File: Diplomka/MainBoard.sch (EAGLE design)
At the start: 29 parts, among them K1 ARK550/2, K2 ARK550/2, Q1 AP2012P3C-P22, Q2 BC817-40LT1SMD, U1 ESP32-WROOM-32, U2 AMS1117-3.3

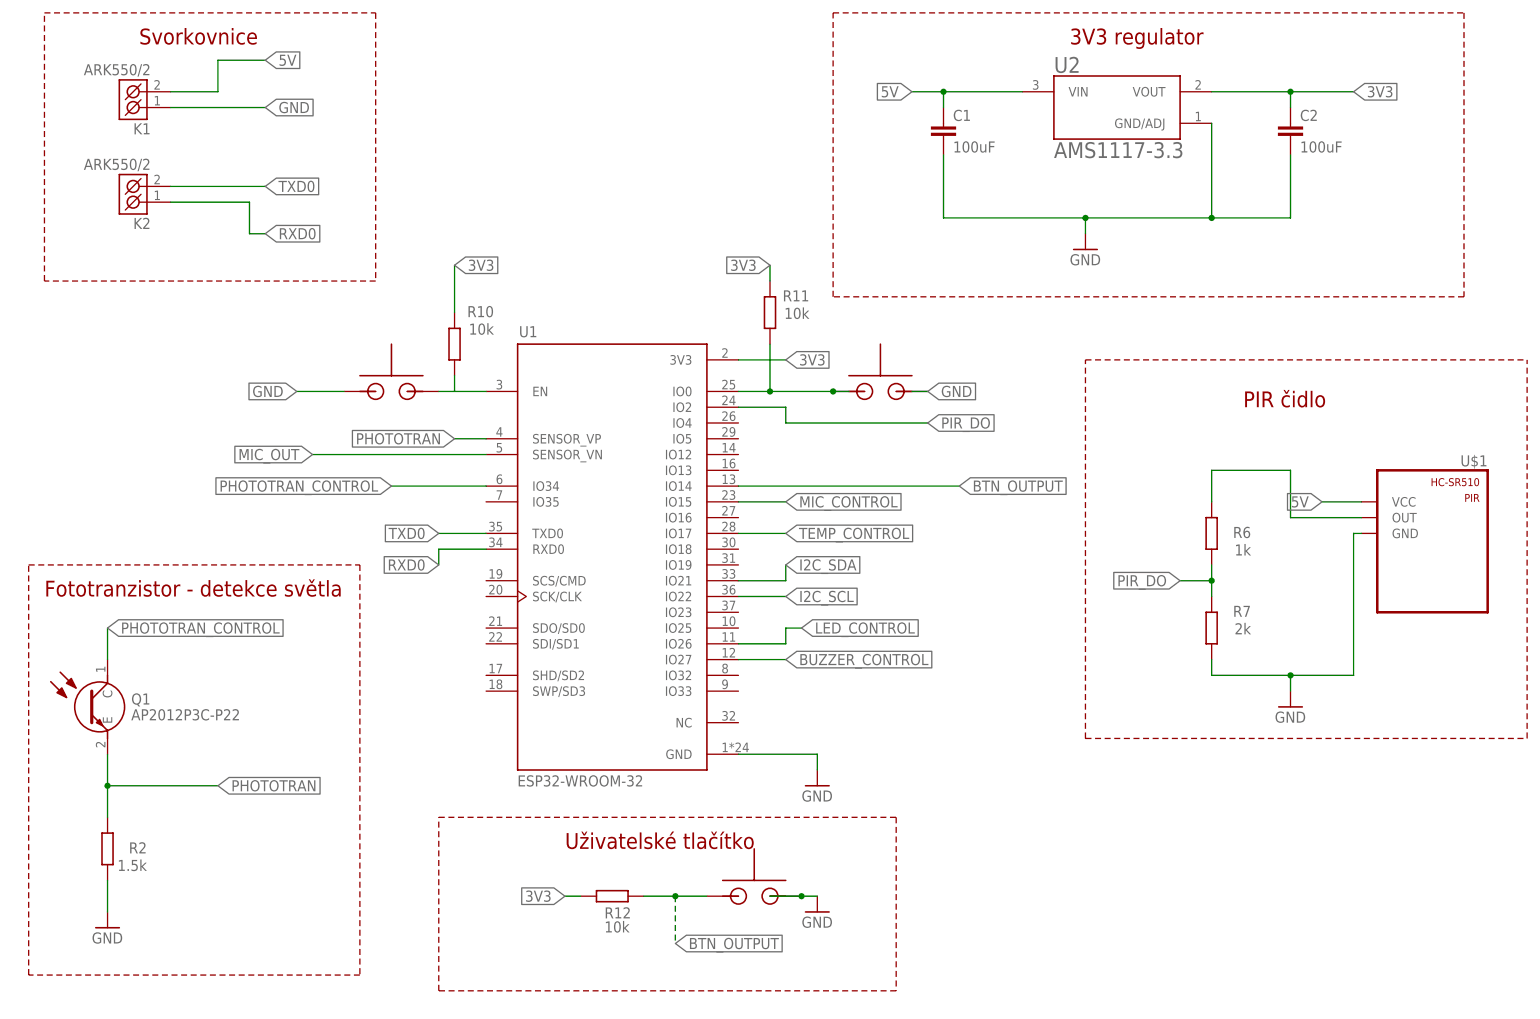
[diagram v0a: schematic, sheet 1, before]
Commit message: Přidány do repozitáře pravidla JLCPCB, nakresleno PCB asi z 70%ˇ.
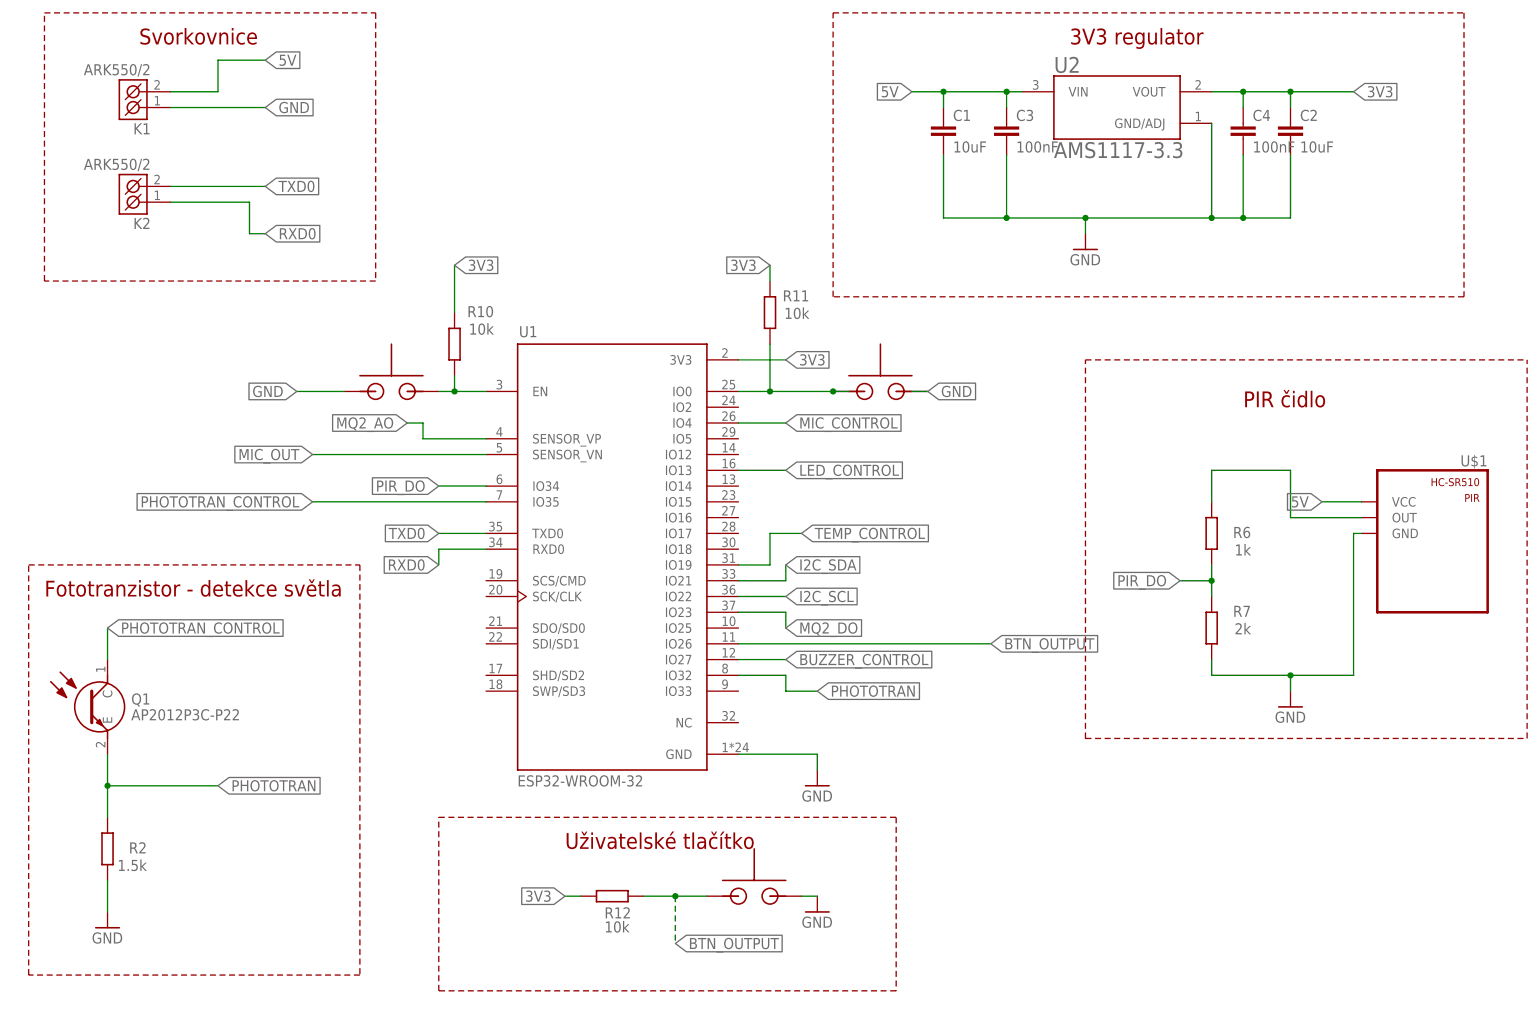
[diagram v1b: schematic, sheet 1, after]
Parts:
- added C3, C4: 100nF, rcl:C-EUC0805
- C1, C2: value 100uF -> 10uF
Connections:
- removed net N$9: R10.1
- net 3V3: now also C4.1; no longer U$3.VCC
- net 5V: now also C3.1
- net BTN_OUTPUT: now also U1.IO26; no longer U1.IO14
- net GND: now also C3.2, C4.2
- net LED_CONTROL: now also U1.IO13; no longer U1.IO26
- net MIC_CONTROL: now also U$3.VCC, U1.IO4; no longer U$3.OUT, U1.IO15
- net MIC_OUT: now also U$3.OUT
- net MQ2_AO: now also U1.SENSOR_VP
- net MQ2_DO: now also U1.IO23
- net N$7: now also R10.1
- net PHOTOTRAN: now also U1.IO32; no longer U1.SENSOR_VP
- net PHOTOTRAN_CONTROL: now also U1.IO35; no longer U1.IO34
- net PIR_DO: now also U1.IO34; no longer U1.IO2
- net TEMP_CONTROL: now also U1.IO19; no longer U1.IO17

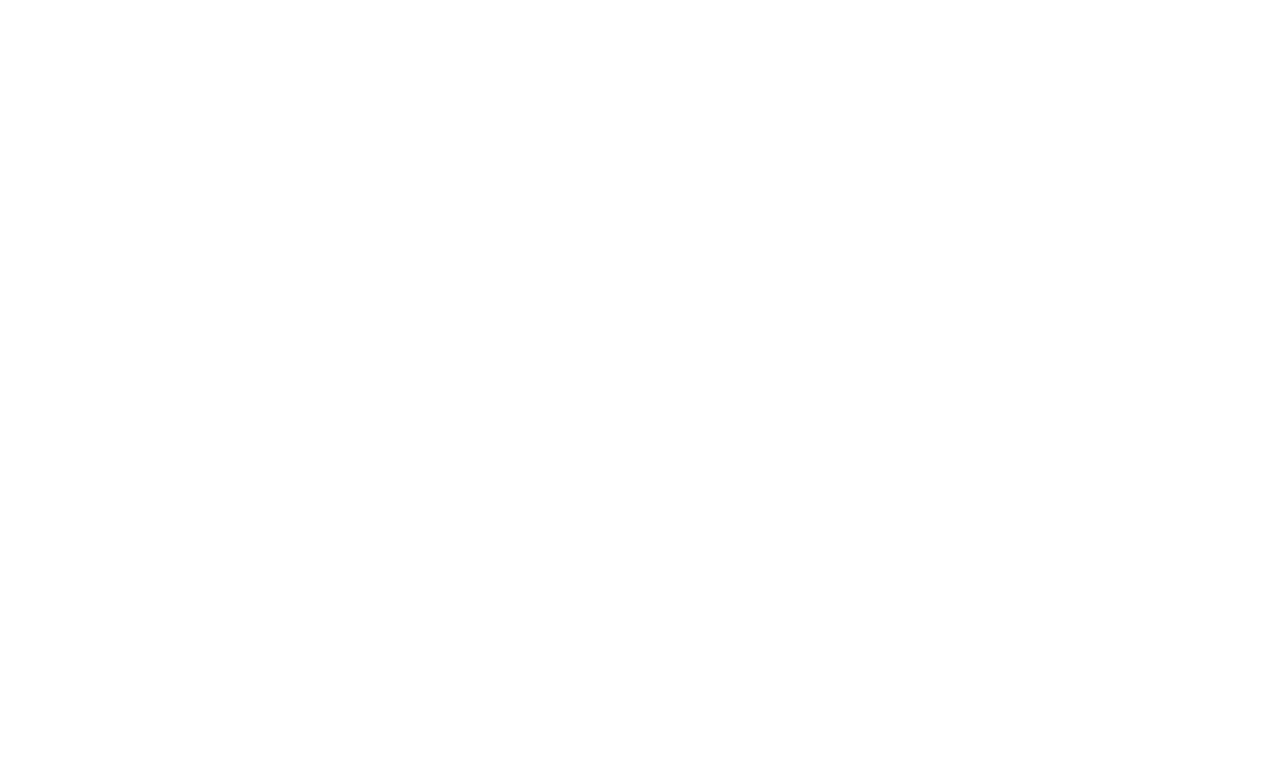
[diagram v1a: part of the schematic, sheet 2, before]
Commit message: Přidán stepdown converted. Třeba dodat vhodnou cívku a dokreslit desku.
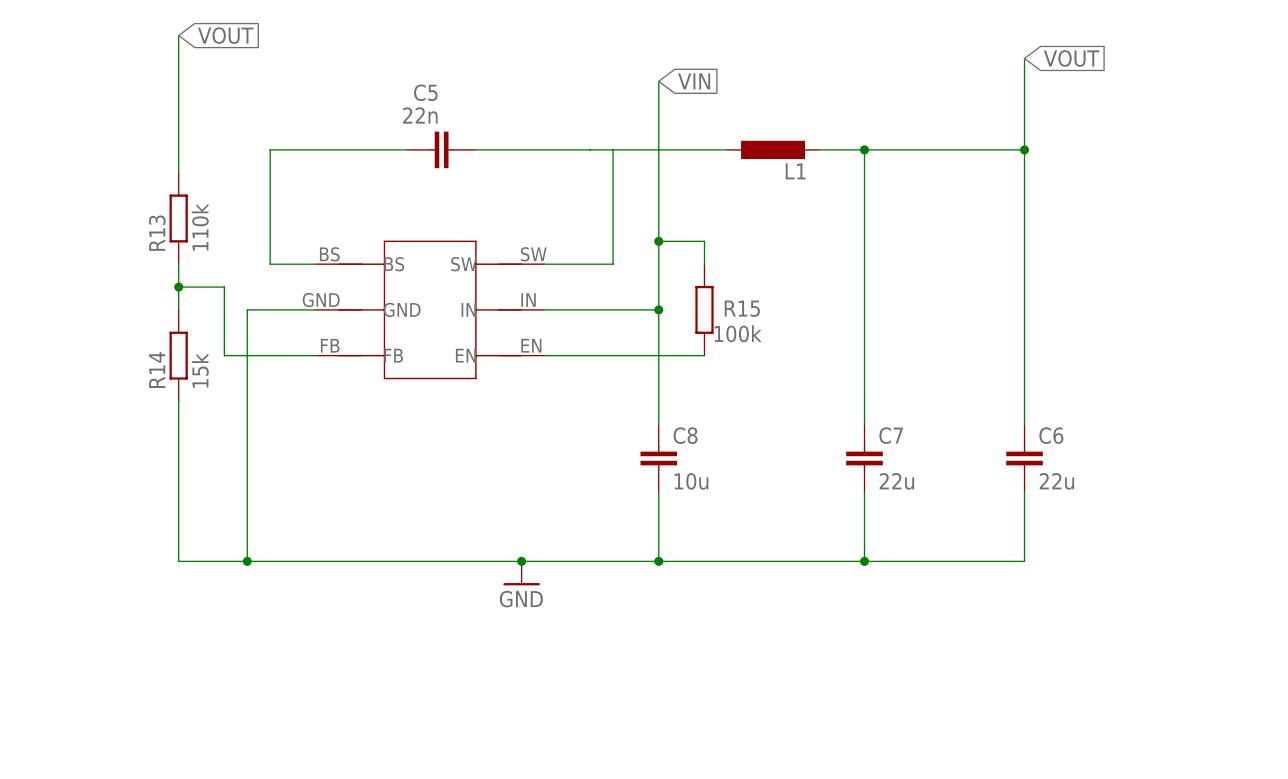
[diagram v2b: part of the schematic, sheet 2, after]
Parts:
- added C5: 22n, rcl:C-EUC0805
- added C6, C7: 22u, rcl:C-EUC0805
- added C8: 10u, rcl:C-EUC0805
- added L1: (no value), rcl:L-EUL3225M
- added R13: 110k, rcl:R-EU_R0805
- added R14: 15k, rcl:R-EU_R0805
- added R15: 100k, rcl:R-EU_R0805
- added U$9: SD8942, myParts:SD8942
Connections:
- new net N$10: C5.2, L1.1, U$9.SW
- new net N$11: R15.1, U$9.EN
- new net N$12: R13.1, R14.2, U$9.FB
- new net N$9: C5.1, U$9.BS
- new net VIN: C8.1, R15.2, U$9.IN
- new net VOUT: C6.1, C7.1, L1.2, R13.2
- net GND: now also C6.2, C7.2, C8.2, R14.1, U$9.GND
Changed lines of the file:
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@@
 <part name="C3" library="rcl" library_urn="urn:adsk.eagle:library:334" deviceset="C-EU" device="C0805" package3d_urn="urn:adsk.eagle:package:23617/2" value="100nF"/>
 <part name="C4" library="rcl" library_urn="urn:adsk.eagle:library:334" deviceset="C-EU" device="C0805" package3d_urn="urn:adsk.eagle:package:23617/2" value="100nF"/>
+<part name="U$9" library="myParts" deviceset="SD8942" device=""/>
+<part name="C5" library="rcl" library_urn="urn:adsk.eagle:library:334" deviceset="C-EU" device="C0805" package3d_urn="urn:adsk.eagle:package:23617/2" value="22n"/>
+<part name="C6" library="rcl" library_urn="urn:adsk.eagle:library:334" deviceset="C-EU" device="C0805" package3d_urn="urn:adsk.eagle:package:23617/2" value="22u"/>
+<part name="C7" library="rcl" library_urn="urn:adsk.eagle:library:334" deviceset="C-EU" device="C0805" package3d_urn="urn:adsk.eagle:package:23617/2" value="22u"/>
+<part name="C8" library="rcl" library_urn="urn:adsk.eagle:library:334" deviceset="C-EU" device="C0805" package3d_urn="urn:adsk.eagle:package:23617/2" value="10u"/>
+<part name="R13" library="rcl" library_urn="urn:adsk.eagle:library:334" deviceset="R-EU_" device="R0805" package3d_urn="urn:adsk.eagle:package:23553/2" value="110k"/>
+<part name="R14" library="rcl" library_urn="urn:adsk.eagle:library:334" deviceset="R-EU_" device="R0805" package3d_urn="urn:adsk.eagle:package:23553/2" value="15k"/>
+<part name="R15" library="rcl" library_urn="urn:adsk.eagle:library:334" deviceset="R-EU_" device="R0805" package3d_urn="urn:adsk.eagle:package:23553/2" value="100k"/>
+<part name="L1" library="rcl" library_urn="urn:adsk.eagle:library:334" deviceset="L-EU" device="L3225M" package3d_urn="urn:adsk.eagle:package:23477/2"/>
+<part name="GND9" library="supply1" library_urn="urn:adsk.eagle:library:371" deviceset="GND" device=""/>
 </parts>
 <sheets>
@@
 </instance>
 <instance part="U$5" gate="G$1" x="58.42" y="119.38" smashed="yes"/>
+<instance part="U$9" gate="G$1" x="27.94" y="220.98" smashed="yes"/>
+<instance part="C5" gate="G$1" x="27.94" y="238.76" smashed="yes" rot="R90">
+<attribute name="NAME" x="28.956" y="245.999" size="1.778" layer="95" rot="R180"/>
+<attribute name="VALUE" x="28.956" y="243.459" size="1.778" layer="96" rot="R180"/>
+</instance>
+<instance part="C6" gate="G$1" x="93.98" y="205.74" smashed="yes">
+<attribute name="NAME" x="95.504" y="206.121" size="1.778" layer="95"/>
+<attribute name="VALUE" x="95.504" y="201.041" size="1.778" layer="96"/>
+</instance>
+<instance part="C7" gate="G$1" x="76.2" y="205.74" smashed="yes">
+<attribute name="NAME" x="77.724" y="206.121" size="1.778" layer="95"/>
+<attribute name="VALUE" x="77.724" y="201.041" size="1.778" layer="96"/>
+</instance>
+<instance part="C8" gate="G$1" x="53.34" y="205.74" smashed="yes">
+<attribute name="NAME" x="54.864" y="206.121" size="1.778" layer="95"/>
+<attribute name="VALUE" x="54.864" y="201.041" size="1.778" layer="96"/>
+</instance>
+<instance part="R13" gate="G$1" x="0" y="231.14" smashed="yes" rot="R90">
+<attribute name="NAME" x="-1.4986" y="227.33" size="1.778" layer="95" rot="R90"/>
+<attribute name="VALUE" x="3.302" y="227.33" size="1.778" layer="96" rot="R90"/>
+</instance>
+<instance part="R14" gate="G$1" x="0" y="215.9" smashed="yes" rot="R90">
+<attribute name="NAME" x="-1.4986" y="212.09" size="1.778" layer="95" rot="R90"/>
+<attribute name="VALUE" x="3.302" y="212.09" size="1.778" layer="96" rot="R90"/>
+</instance>
+<instance part="R15" gate="G$1" x="58.42" y="220.98" smashed="yes" rot="R90">
+<attribute name="NAME" x="64.77" y="222.0214" size="1.778" layer="95" rot="R180"/>
+<attribute name="VALUE" x="64.77" y="219.202" size="1.778" layer="96" rot="R180"/>
+</instance>
+<instance part="L1" gate="G$1" x="66.04" y="238.76" smashed="yes" rot="R90">
+<attribute name="NAME" x="69.85" y="237.2614" size="1.778" layer="95" rot="R180"/>
+<attribute name="VALUE" x="69.85" y="242.062" size="1.778" layer="96" rot="R180"/>
+</instance>
+<instance part="GND9" gate="1" x="38.1" y="190.5" smashed="yes">
+<attribute name="VALUE" x="35.56" y="187.96" size="1.778" layer="96"/>
+</instance>
 </instances>
 <busses>
@@
 <label x="20.32" y="119.38" size="1.778" layer="95" rot="R180" xref="yes"/>
 </segment>
+<segment>
+<pinref part="R14" gate="G$1" pin="1"/>
+<pinref part="GND9" gate="1" pin="GND"/>
+<wire x1="0" y1="210.82" x2="0" y2="193.04" width="0.1524" layer="91"/>
+<wire x1="0" y1="193.04" x2="7.62" y2="193.04" width="0.1524" layer="91"/>
+<pinref part="C8" gate="G$1" pin="2"/>
+<wire x1="7.62" y1="193.04" x2="38.1" y2="193.04" width="0.1524" layer="91"/>
+<wire x1="38.1" y1="193.04" x2="53.34" y2="193.04" width="0.1524" layer="91"/>
+<wire x1="53.34" y1="193.04" x2="53.34" y2="200.66" width="0.1524" layer="91"/>
+<junction x="38.1" y="193.04"/>
+<pinref part="C7" gate="G$1" pin="2"/>
+<wire x1="53.34" y1="193.04" x2="76.2" y2="193.04" width="0.1524" layer="91"/>
+<wire x1="76.2" y1="193.04" x2="76.2" y2="200.66" width="0.1524" layer="91"/>
+<junction x="53.34" y="193.04"/>
+<pinref part="C6" gate="G$1" pin="2"/>
+<wire x1="76.2" y1="193.04" x2="93.98" y2="193.04" width="0.1524" layer="91"/>
+<wire x1="93.98" y1="193.04" x2="93.98" y2="200.66" width="0.1524" layer="91"/>
+<junction x="76.2" y="193.04"/>
+<pinref part="U$9" gate="G$1" pin="GND"/>
+<wire x1="15.24" y1="220.98" x2="7.62" y2="220.98" width="0.1524" layer="91"/>
+<wire x1="7.62" y1="220.98" x2="7.62" y2="193.04" width="0.1524" layer="91"/>
+<junction x="7.62" y="193.04"/>
+</segment>
 </net>
 <net name="N$3" class="0">
@@
 </segment>
 </net>
+<net name="N$9" class="0">
+<segment>
+<pinref part="U$9" gate="G$1" pin="BS"/>
+<wire x1="15.24" y1="226.06" x2="10.16" y2="226.06" width="0.1524" layer="91"/>
+<wire x1="10.16" y1="226.06" x2="10.16" y2="238.76" width="0.1524" layer="91"/>
+<pinref part="C5" gate="G$1" pin="1"/>
+<wire x1="10.16" y1="238.76" x2="25.4" y2="238.76" width="0.1524" layer="91"/>
+</segment>
+</net>
+<net name="N$10" class="0">
+<segment>
+<wire x1="48.26" y1="238.76" x2="48.26" y2="226.06" width="0.1524" layer="91"/>
+<pinref part="U$9" gate="G$1" pin="SW"/>
+<wire x1="48.26" y1="226.06" x2="40.64" y2="226.06" width="0.1524" layer="91"/>
+<pinref part="C5" gate="G$1" pin="2"/>
+<wire x1="33.02" y1="238.76" x2="45.72" y2="238.76" width="0.1524" layer="91"/>
+<pinref part="L1" gate="G$1" pin="1"/>
+<wire x1="45.72" y1="238.76" x2="48.26" y2="238.76" width="0.1524" layer="91"/>
+<wire x1="60.96" y1="238.76" x2="48.26" y2="238.76" width="0.1524" layer="91"/>
+</segment>
+</net>
+<net name="N$11" class="0">
+<segment>
+<pinref part="U$9" gate="G$1" pin="EN"/>
+<pinref part="R15" gate="G$1" pin="1"/>
+<wire x1="40.64" y1="215.9" x2="58.42" y2="215.9" width="0.1524" layer="91"/>
+</segment>
+</net>
+<net name="VIN" class="0">
+<segment>
+<pinref part="R15" gate="G$1" pin="2"/>
+<wire x1="58.42" y1="226.06" x2="58.42" y2="228.6" width="0.1524" layer="91"/>
+<wire x1="58.42" y1="228.6" x2="53.34" y2="228.6" width="0.1524" layer="91"/>
+<wire x1="53.34" y1="228.6" x2="53.34" y2="246.38" width="0.1524" layer="91"/>
+<label x="53.34" y="246.38" size="1.778" layer="95" xref="yes"/>
+<pinref part="C8" gate="G$1" pin="1"/>
+<pinref part="U$9" gate="G$1" pin="IN"/>
+<wire x1="53.34" y1="208.28" x2="53.34" y2="220.98" width="0.1524" layer="91"/>
+<wire x1="53.34" y1="220.98" x2="40.64" y2="220.98" width="0.1524" layer="91"/>
+<wire x1="53.34" y1="220.98" x2="53.34" y2="228.6" width="0.1524" layer="91"/>
+<junction x="53.34" y="220.98"/>
+<junction x="53.34" y="228.6"/>
+</segment>
+</net>
+<net name="N$12" class="0">
+<segment>
+<pinref part="R14" gate="G$1" pin="2"/>
+<pinref part="R13" gate="G$1" pin="1"/>
+<wire x1="0" y1="220.98" x2="0" y2="223.52" width="0.1524" layer="91"/>
+<pinref part="U$9" gate="G$1" pin="FB"/>
+<wire x1="0" y1="223.52" x2="0" y2="226.06" width="0.1524" layer="91"/>
+<wire x1="15.24" y1="215.9" x2="5.08" y2="215.9" width="0.1524" layer="91"/>
+<wire x1="5.08" y1="215.9" x2="5.08" y2="223.52" width="0.1524" layer="91"/>
+<wire x1="5.08" y1="223.52" x2="0" y2="223.52" width="0.1524" layer="91"/>
+<junction x="0" y="223.52"/>
+</segment>
+</net>
+<net name="VOUT" class="0">
+<segment>
+<pinref part="R13" gate="G$1" pin="2"/>
+<wire x1="0" y1="236.22" x2="0" y2="251.46" width="0.1524" layer="91"/>
+<label x="0" y="251.46" size="1.778" layer="95" xref="yes"/>
+</segment>
+<segment>
+<pinref part="C7" gate="G$1" pin="1"/>
+<pinref part="L1" gate="G$1" pin="2"/>
+<wire x1="76.2" y1="208.28" x2="76.2" y2="238.76" width="0.1524" layer="91"/>
+<wire x1="76.2" y1="238.76" x2="71.12" y2="238.76" width="0.1524" layer="91"/>
+<pinref part="C6" gate="G$1" pin="1"/>
+<wire x1="93.98" y1="208.28" x2="93.98" y2="238.76" width="0.1524" layer="91"/>
+<wire x1="93.98" y1="238.76" x2="76.2" y2="238.76" width="0.1524" layer="91"/>
+<junction x="76.2" y="238.76"/>
+<wire x1="93.98" y1="238.76" x2="93.98" y2="248.92" width="0.1524" layer="91"/>
+<junction x="93.98" y="238.76"/>
+<label x="93.98" y="248.92" size="1.778" layer="95" xref="yes"/>
+</segment>
+</net>

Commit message: Cca hotový plošňák, třeba udělat nějaké úpravy ale jinak dobré.
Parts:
- removed K2: ARK550/2, #PaJa_konektory:ARK550/2
- added JUM1: S1G6_JUMP, #PaJa_konektory:S1G6_JUMP
- added Q3, Q4: SS8050-G, SS8050-G:SS8050-G
- added R16, R17: (no value), rcl:R-EU_R0805
- C8: value 10u -> 10u/25V
- L1: value (none) -> SRR1260-4R7Y; device rcl:L-EUL3225M -> SRR1260-4R7Y:SRR1260-4R7Y
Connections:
- removed net N$7: R10.1, U$6.+, U1.EN
- removed net N$8: R11.1, U$7.+, U1.IO0
- removed net RXD0: K2.K1, U1.RXD0
- removed net TXD0: K2.K2, U1.TXD0
- removed net VOUT: C6.1, C7.1, L1.2, R13.2
- new net CTS: JUM1.5, Q4.B, R17.2
- new net DTR: JUM1.1, Q4.E, R16.1
- new net EN: Q3.C, R10.1, U$6.+, U1.EN
- new net IO0: Q4.C, R11.1, U$7.+, U1.IO0
- new net N$13: Q3.B, R16.2
- new net N$15: Q3.E, R17.1
- new net UART_PC_RX: JUM1.2, U1.TXD0
- new net UART_PC_TX: JUM1.3, U1.RXD0
- new net VCC: JUM1.4
- net 5V: now also C6.1, C7.1, L1.2, R13.2; no longer K1.K2
- net GND: now also JUM1.6
- net VIN: now also K1.K2
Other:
- note added: "ESP32 programmer reset"
- note added: "Step down převodník pro 5V"
